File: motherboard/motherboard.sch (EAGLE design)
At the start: 8 parts, among them U1 LED_100V_BUCK, U2 LED_100V_BUCK, U3 LED_100V_BUCK, U4 LED_100V_BUCK

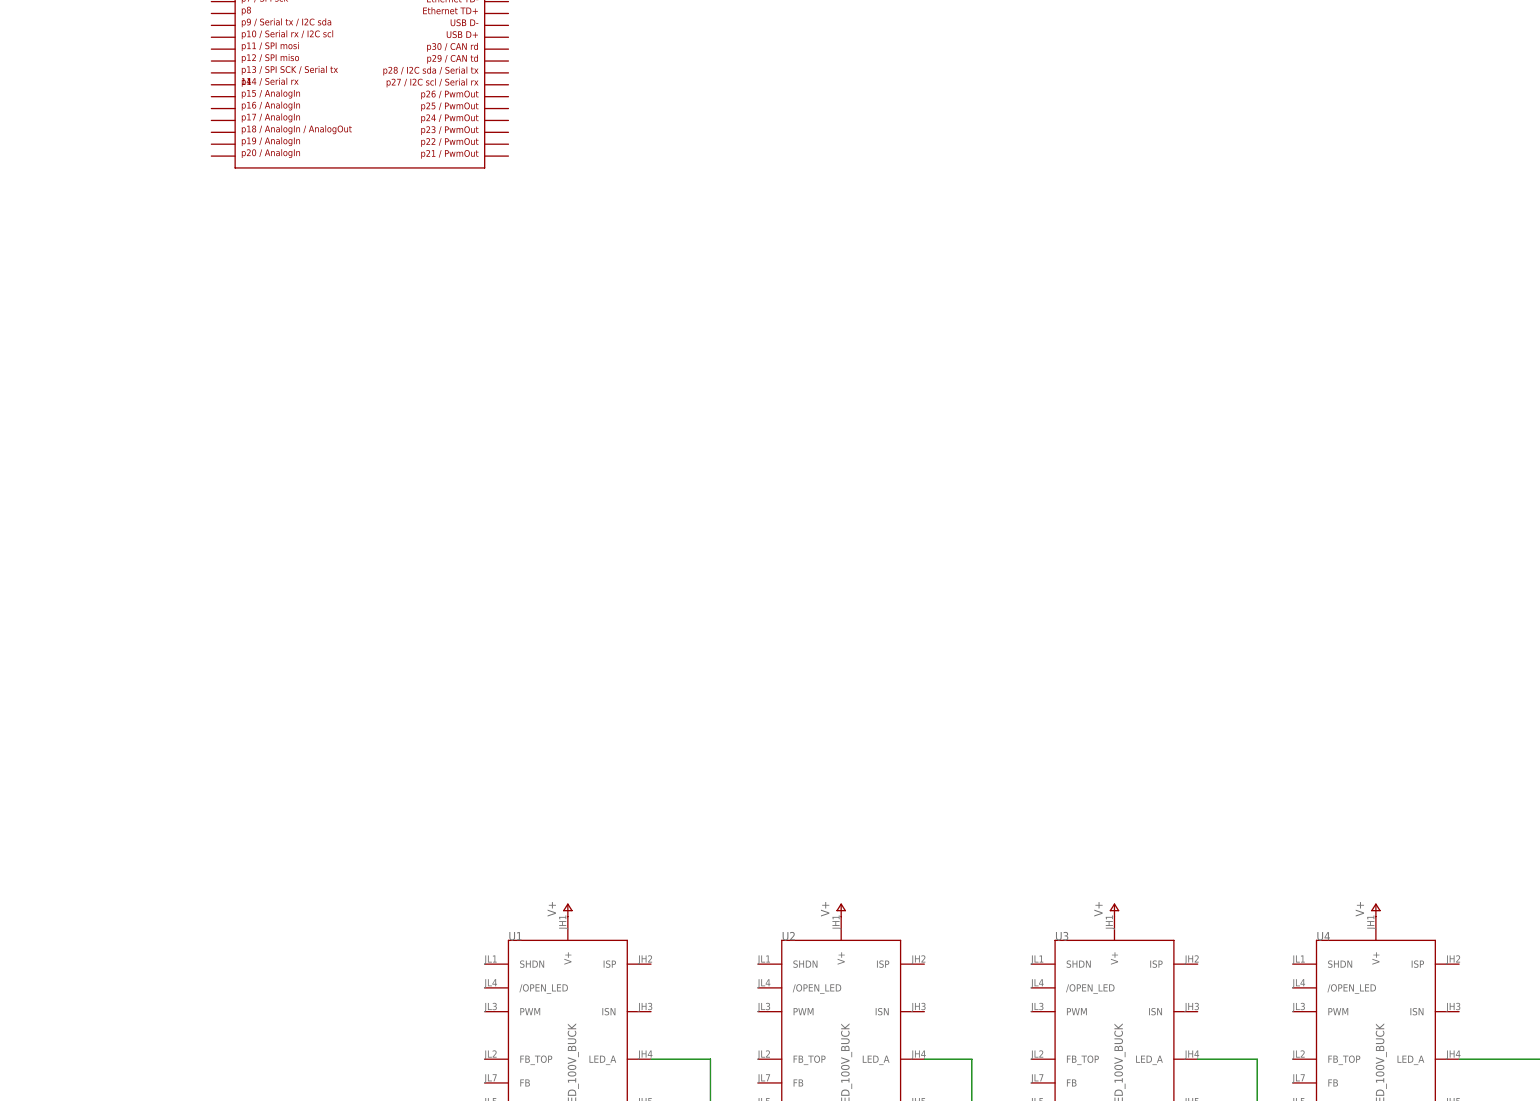
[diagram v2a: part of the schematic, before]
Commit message: Added signals between led drivers and mcu, still need voltage feedback
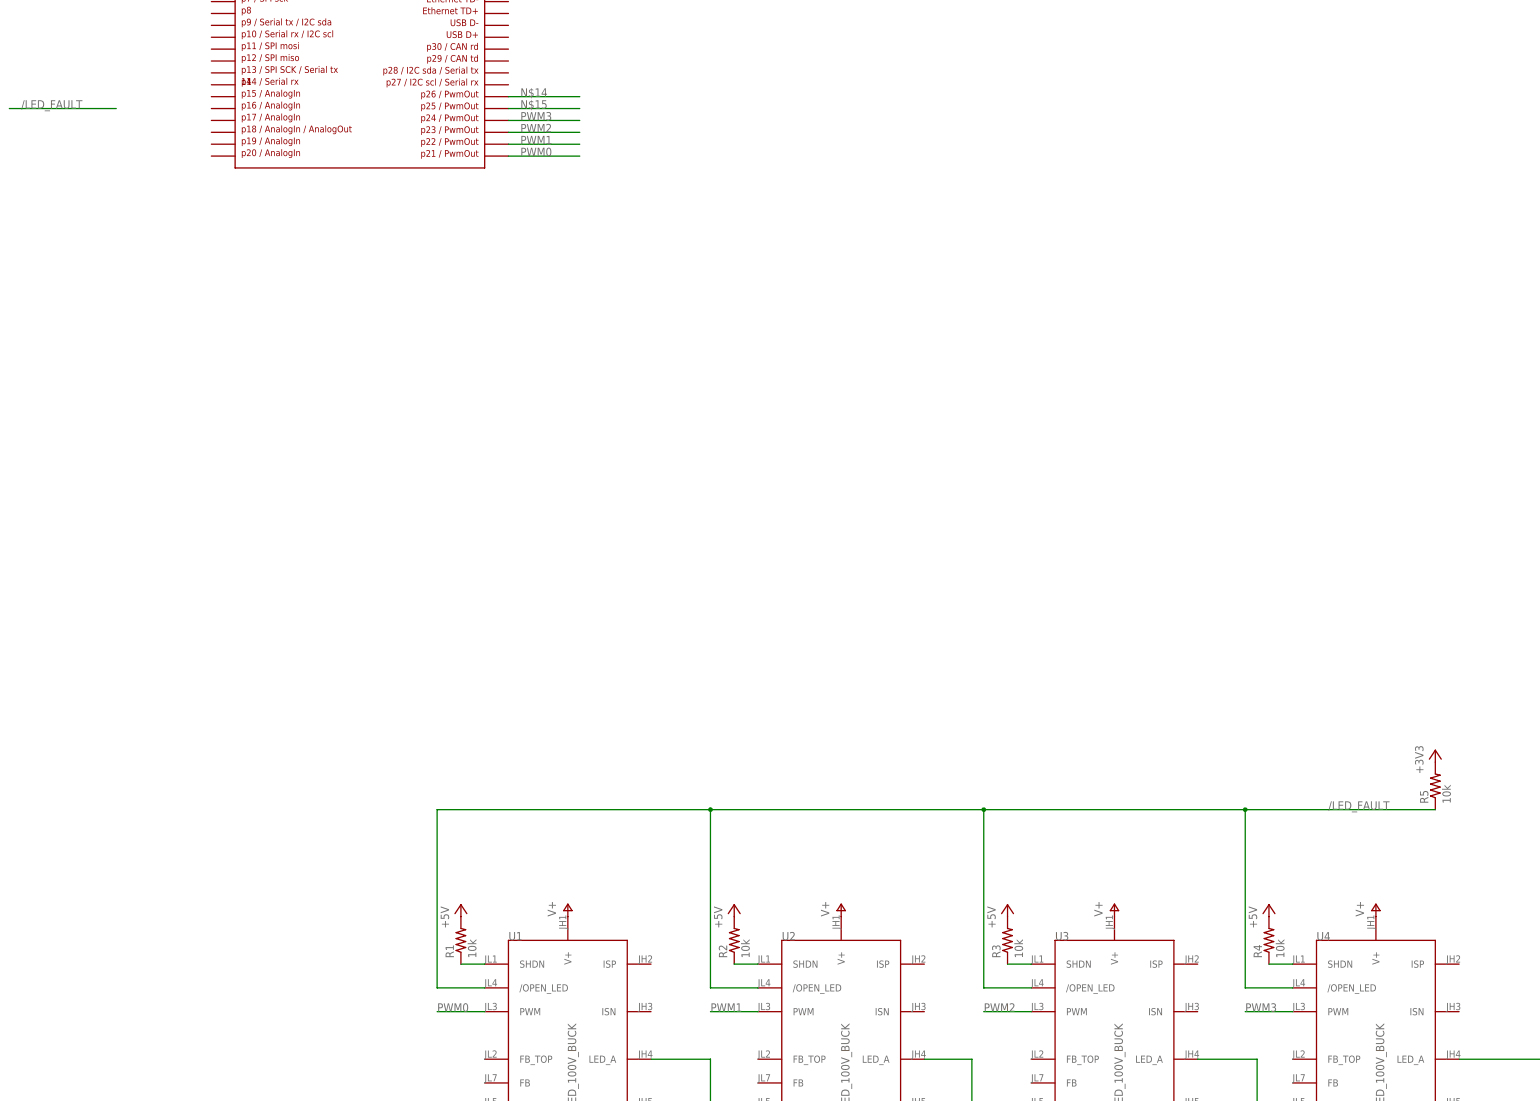
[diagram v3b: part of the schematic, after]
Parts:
- added R1, R2, R3, R4, R5: 10k, rcl:R-US_0204/5
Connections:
- new net /LED_FAULT: R5.1, U1./OPEN_LED, U2./OPEN_LED, U3./OPEN_LED, U4./OPEN_LED
- new net N$10: R1.1, U1.SHDN
- new net N$11: R3.1, U3.SHDN
- new net N$12: R4.1, U4.SHDN
- new net N$13: R2.1, U2.SHDN
- new net N$14: U$1.P$26
- new net N$15: U$1.P$25
- new net PWM0: U$1.P$21, U1.PWM
- new net PWM1: U$1.P$22, U2.PWM
- new net PWM2: U$1.P$23, U3.PWM
- new net PWM3: U$1.P$24, U4.PWM
- net +3V3: now also R5.2
- net +5V: now also R1.2, R2.2, R3.2, R4.2
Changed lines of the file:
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@@
 <?xml version="1.0" encoding="utf-8"?>
 <!DOCTYPE eagle SYSTEM "eagle.dtd">
-<eagle version="6.2">
+<eagle version="6.1">
 <drawing>
 <settings>
@@
 <part name="+3V1" library="supply1" deviceset="+3V3" device=""/>
 <part name="P+6" library="supply1" deviceset="+5V" device=""/>
+<part name="R1" library="rcl" deviceset="R-US_" device="0204/5" value="10k"/>
+<part name="P+1" library="supply1" deviceset="+5V" device=""/>
+<part name="R2" library="rcl" deviceset="R-US_" device="0204/5" value="10k"/>
+<part name="P+7" library="supply1" deviceset="+5V" device=""/>
+<part name="R3" library="rcl" deviceset="R-US_" device="0204/5" value="10k"/>
+<part name="R4" library="rcl" deviceset="R-US_" device="0204/5" value="10k"/>
+<part name="P+8" library="supply1" deviceset="+5V" device=""/>
+<part name="P+9" library="supply1" deviceset="+5V" device=""/>
+<part name="R5" library="rcl" deviceset="R-US_" device="0204/5" value="10k"/>
+<part name="+3V2" library="supply1" deviceset="+3V3" device=""/>
 </parts>
 <sheets>
@@
 <instance part="+3V1" gate="G$1" x="43.18" y="292.1" rot="R270"/>
 <instance part="P+6" gate="1" x="-50.8" y="289.56" rot="R90"/>
+<instance part="R1" gate="G$1" x="15.24" y="76.2" rot="R90"/>
+<instance part="P+1" gate="1" x="15.24" y="83.82"/>
+<instance part="R2" gate="G$1" x="73.66" y="76.2" rot="R90"/>
+<instance part="P+7" gate="1" x="73.66" y="83.82"/>
+<instance part="R3" gate="G$1" x="132.08" y="76.2" rot="R90"/>
+<instance part="R4" gate="G$1" x="187.96" y="76.2" rot="R90"/>
+<instance part="P+8" gate="1" x="132.08" y="83.82"/>
+<instance part="P+9" gate="1" x="187.96" y="83.82"/>
+<instance part="R5" gate="G$1" x="223.52" y="109.22" rot="R90"/>
+<instance part="+3V2" gate="G$1" x="223.52" y="116.84"/>
 </instances>
 <busses>
@@
 <wire x1="40.64" y1="292.1" x2="25.4" y2="292.1" width="0.1524" layer="91"/>
 </segment>
+<segment>
+<pinref part="R5" gate="G$1" pin="2"/>
+<pinref part="+3V2" gate="G$1" pin="+3V3"/>
+</segment>
 </net>
 <net name="+5V" class="0">
@@
 <pinref part="P+6" gate="1" pin="+5V"/>
 </segment>
-</net>
+<segment>
+<pinref part="R1" gate="G$1" pin="2"/>
+<pinref part="P+1" gate="1" pin="+5V"/>
+</segment>
+<segment>
+<pinref part="R2" gate="G$1" pin="2"/>
+<pinref part="P+7" gate="1" pin="+5V"/>
+</segment>
+<segment>
+<pinref part="R3" gate="G$1" pin="2"/>
+<pinref part="P+8" gate="1" pin="+5V"/>
+</segment>
+<segment>
+<pinref part="R4" gate="G$1" pin="2"/>
+<pinref part="P+9" gate="1" pin="+5V"/>
+</segment>
+</net>
+<net name="N$10" class="0">
+<segment>
+<pinref part="U1" gate="G$1" pin="SHDN"/>
+<pinref part="R1" gate="G$1" pin="1"/>
+<wire x1="15.24" y1="71.12" x2="20.32" y2="71.12" width="0.1524" layer="91"/>
+</segment>
+</net>
+<net name="N$11" class="0">
+<segment>
+<pinref part="U3" gate="G$1" pin="SHDN"/>
+<pinref part="R3" gate="G$1" pin="1"/>
+<wire x1="132.08" y1="71.12" x2="137.16" y2="71.12" width="0.1524" layer="91"/>
+</segment>
+</net>
+<net name="N$12" class="0">
+<segment>
+<pinref part="U4" gate="G$1" pin="SHDN"/>
+<pinref part="R4" gate="G$1" pin="1"/>
+<wire x1="187.96" y1="71.12" x2="193.04" y2="71.12" width="0.1524" layer="91"/>
+</segment>
+</net>
+<net name="N$13" class="0">
+<segment>
+<pinref part="R2" gate="G$1" pin="1"/>
+<pinref part="U2" gate="G$1" pin="SHDN"/>
+<wire x1="73.66" y1="71.12" x2="78.74" y2="71.12" width="0.1524" layer="91"/>
+</segment>
+</net>
+<net name="/LED_FAULT" class="0">
+<segment>
+<pinref part="U3" gate="G$1" pin="/OPEN_LED"/>
+<wire x1="137.16" y1="66.04" x2="127" y2="66.04" width="0.1524" layer="91"/>
+<wire x1="127" y1="66.04" x2="127" y2="104.14" width="0.1524" layer="91"/>
+<pinref part="R5" gate="G$1" pin="1"/>
+<wire x1="223.52" y1="104.14" x2="182.88" y2="104.14" width="0.1524" layer="91"/>
+<pinref part="U4" gate="G$1" pin="/OPEN_LED"/>
+<wire x1="182.88" y1="104.14" x2="127" y2="104.14" width="0.1524" layer="91"/>
+<wire x1="193.04" y1="66.04" x2="182.88" y2="66.04" width="0.1524" layer="91"/>
+<wire x1="182.88" y1="66.04" x2="182.88" y2="104.14" width="0.1524" layer="91"/>
+<pinref part="U2" gate="G$1" pin="/OPEN_LED"/>
+<wire x1="78.74" y1="66.04" x2="68.58" y2="66.04" width="0.1524" layer="91"/>
+<wire x1="68.58" y1="66.04" x2="68.58" y2="104.14" width="0.1524" layer="91"/>
+<wire x1="68.58" y1="104.14" x2="127" y2="104.14" width="0.1524" layer="91"/>
+<pinref part="U1" gate="G$1" pin="/OPEN_LED"/>
+<wire x1="20.32" y1="66.04" x2="10.16" y2="66.04" width="0.1524" layer="91"/>
+<wire x1="10.16" y1="66.04" x2="10.16" y2="104.14" width="0.1524" layer="91"/>
+<wire x1="10.16" y1="104.14" x2="68.58" y2="104.14" width="0.1524" layer="91"/>
+<junction x="68.58" y="104.14"/>
+<junction x="127" y="104.14"/>
+<junction x="182.88" y="104.14"/>
+<label x="200.66" y="104.14" size="1.778" layer="95"/>
+</segment>
+<segment>
+<wire x1="-81.28" y1="254" x2="-58.42" y2="254" width="0.1524" layer="91"/>
+<label x="-78.74" y="254" size="1.778" layer="95"/>
+</segment>
+</net>
+<net name="PWM0" class="0">
+<segment>
+<pinref part="U1" gate="G$1" pin="PWM"/>
+<wire x1="20.32" y1="60.96" x2="10.16" y2="60.96" width="0.1524" layer="91"/>
+<label x="10.16" y="60.96" size="1.778" layer="95"/>
+</segment>
+<segment>
+<pinref part="U$1" gate="G$1" pin="P$21"/>
+<wire x1="25.4" y1="243.84" x2="40.64" y2="243.84" width="0.1524" layer="91"/>
+<label x="27.94" y="243.84" size="1.778" layer="95"/>
+</segment>
+</net>
+<net name="PWM1" class="0">
+<segment>
+<pinref part="U2" gate="G$1" pin="PWM"/>
+<wire x1="78.74" y1="60.96" x2="68.58" y2="60.96" width="0.1524" layer="91"/>
+<label x="68.58" y="60.96" size="1.778" layer="95"/>
+</segment>
+<segment>
+<pinref part="U$1" gate="G$1" pin="P$22"/>
+<wire x1="25.4" y1="246.38" x2="40.64" y2="246.38" width="0.1524" layer="91"/>
+<label x="27.94" y="246.38" size="1.778" layer="95"/>
+</segment>
+</net>
+<net name="PWM2" class="0">
+<segment>
+<pinref part="U3" gate="G$1" pin="PWM"/>
+<wire x1="137.16" y1="60.96" x2="127" y2="60.96" width="0.1524" layer="91"/>
+<label x="127" y="60.96" size="1.778" layer="95"/>
+</segment>
+<segment>
+<pinref part="U$1" gate="G$1" pin="P$23"/>
+<wire x1="25.4" y1="248.92" x2="40.64" y2="248.92" width="0.1524" layer="91"/>
+<label x="27.94" y="248.92" size="1.778" layer="95"/>
+</segment>
+</net>
+<net name="PWM3" class="0">
+<segment>
+<pinref part="U4" gate="G$1" pin="PWM"/>
+<wire x1="193.04" y1="60.96" x2="182.88" y2="60.96" width="0.1524" layer="91"/>
+<label x="182.88" y="60.96" size="1.778" layer="95"/>
+</segment>
+<segment>
+<pinref part="U$1" gate="G$1" pin="P$24"/>
+<wire x1="25.4" y1="251.46" x2="40.64" y2="251.46" width="0.1524" layer="91"/>
+<label x="27.94" y="251.46" size="1.778" layer="95"/>
+</segment>
+</net>
+<net name="N$14" class="0">
+<segment>
+<pinref part="U$1" gate="G$1" pin="P$26"/>
+<wire x1="25.4" y1="256.54" x2="40.64" y2="256.54" width="0.1524" layer="91"/>
+<label x="27.94" y="256.54" size="1.778" layer="95"/>
+</segment>
+</net>
+<net name="N$15" class="0">
+<segment>
+<pinref part="U$1" gate="G$1" pin="P$25"/>
+<wire x1="25.4" y1="254" x2="40.64" y2="254" width="0.1524" layer="91"/>
+<label x="27.94" y="254" size="1.778" layer="95"/>
+</segment>
+</net>

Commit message: Complete schematic
This commit uses generic part selections and has no board layout yet.
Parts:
- added BREAKS, CA: (no value), con-amp-quick:M06
- added C1, C2: (no value), rcl:C-US050-024X044
- added CADENCE, DC, FET, REGEN, SPEED: (no value), con-amp-quick:M02
- added D1, D2: 3.3V, SparkFun-DiscreteSemi:DIODE-ZENERPTH
- added F1, F2: (no value), special:FUSE
- added GRIP: (no value), con-amp-quick:M05
- added IC1: USB6B1, st-microelectronics:USB6B1
- added IR, PHOTO, UART: (no value), con-amp-quick:M04
- added MISSILE: (no value), SparkFun-Electromechanical:SWITCH-SPDTPTH
- added OA1: LM358, SparkFun-AnalogIC:LM358
- added Q1: MOSFET-NCHANNELPTH2, SparkFun-DiscreteSemi:MOSFET-NCHANNELPTH2
- added R10: 50K, rcl:R-US_0204/5
- added R11, R12, R6, R7: 5k, rcl:R-US_0204/5
- added R13, R14: 1k, rcl:R-US_0204/5
- added R15, R16, R17: 10k, rcl:R-US_0204/5
- added R8, R9: 100k, SparkFun-Electromechanical:TRIMPOT3362U-2
- added S2, S3: (no value), SparkFun-Electromechanical:TAC_SWITCHPTH
- added SONAR: M05X2PTH, SparkFun-Connectors:M05X2PTH
- added T1, T2: 2N3904, transistor:2N3904
- added X1: USB_3P-85-32003-00X-1, con-cypressindustries:USB_3P-85-32003-00X-1
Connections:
- removed net N$15: U$1.P$25
- new net BATT_SENSE: D1.C, R11.2, R12.1, U$1.P$16
- new net BREAK_L: BREAKS.2, U$1.P$19
- new net BREAK_R: BREAKS.5, U$1.P$20
- new net BTN1: S2.1, S2.2, U$1.P$30
- new net BTN2: S3.1, S3.2, U$1.P$29
- new net CADENCE: CADENCE.1
- new net D+: IC1.IO2@2, U$1.P$31, X1C.3
- new net D-: IC1.IO1@2, U$1.P$32, X1C.2
- new net GRIP_PB: GRIP.4
- new net GRIP_THROTTLE: GRIP.2, U$1.P$17
- new net MOT_CUR: D2.C, OA1G$1.OUT, R8.CW, U$1.P$15
- new net N$16: OA1G$1.-IN, R6.1, R8.WIPER
- new net N$17: OA1G$1.+IN, R7.1
- new net N$18: R10.1, R9.WIPER
- new net N$19: MISSILE.O, OA1G$2.OUT, R9.CW
- new net N$20: OA1G$2.-IN
- new net N$21: F1.2, R11.1
- new net N$22: C2.1, PHOTO.3, R13.2
- new net N$23: C1.1, PHOTO.1, R14.2
- new net N$24: DC.2, F2.1
- new net N$25: REGEN.1, T1.C
- new net N$26: FET.1, Q1.D
- new net PHOTO1: R14.1
- new net PHOTO2: R13.1
- new net REGEN: T1.B, U$1.P$26
- new net SCL: IR.1, R16.2, U$1.P$27
- new net SDA: IR.2, R15.2, U$1.P$28
- new net SERIAL_RX: U$1.P$14, UART.2
- new net SERIAL_TX: U$1.P$13, UART.3
- new net SERVO_PWM: T2.B, U$1.P$25
- new net SHUNT+: CA.4, R7.2
- new net SHUNT-: CA.3, R6.2
- new net SONAR_PULSE1: SONAR.3, U$1.P$11
- new net SONAR_PULSE2: SONAR.4, U$1.P$12
- new net SONAR_TRIGGER1: SONAR.5, SONAR.8
- new net SONAR_TRIGGER2: SONAR.6, SONAR.7
- new net SPEED: SPEED.1
- new net TACHOMETER: CA.5
- new net THROTTLE_OUT: CA.6, MISSILE.P
- new net THROTTLE_OUT_RAW: OA1G$2.+IN, U$1.P$18
- new net VBATT: CA.1, F1.1
- new net VU: IC1.VCC@2, U$1.P$39, X1C.1
- net +3V3: now also BREAKS.1, BREAKS.4, GRIP.1, IR.3, R15.1, R16.1, S2.3, S2.4, S3.3, S3.4, UART.1
- net +5V: now also F2.2, OA1G$1.V+, SONAR.1, SONAR.2, T2.C, X1A.1, X1B.1
- net GND: now also BREAKS.3, BREAKS.6, C1.2, C2.2, CA.2, CADENCE.2, D1.A, D2.A, DC.1, FET.2, GRIP.3, GRIP.5, IC1.GND@2, IR.4, MISSILE.S, OA1G$1.V-, PHOTO.2, PHOTO.4, Q1.S, R10.2, R12.2, R17.1, REGEN.2, SONAR.10, SONAR.9, SPEED.2, T1.E, UART.4, X1A.4, X1B.4, X1C.4
- net N$14: now also Q1.G, R17.2, T2.E; no longer U$1.P$26
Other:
- moved on the sheet: R1, R2, R3, R4, R5, U$3, U1, U2, U3, U4

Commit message: Ready for parts and firmware
Far enough along now to determine the size of the perfboard to put this
on (6" x 6") and to start working on a BOM and firmware. My plan now is
to get a little ways in to the firmware and place the order when I'm
sure the firmware won't require hardware design changes.
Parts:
- removed BREAKS: (no value), con-amp-quick:M06
- removed S1: (no value), SparkFun-Electromechanical:TAC_SWITCHPTH
- added PTC1, PTC2, PTC3: (no value), ptc-ntc:PTC679
- added X_BREAK_L, X_BREAK_R: (no value), SparkFun-Connectors:M03JST-PTH
- CADENCE, DC, FET, REGEN, SPEED: device con-amp-quick:M02 -> SparkFun-Connectors:M02JST-PTH-2-KIT
- F1: value (none) -> PTCPTH; device special:FUSE -> SparkFun-PowerIC:PTCPTH
- PHOTO, UART: device con-amp-quick:M04 -> SparkFun-Connectors:M04JST-PTH
- renumbered U$3 to LEDS
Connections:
- new net N$15: PTC2.2, X1A.1
- new net N$27: PTC3.2, X1B.1
- net +3V3: now also UART.4, X_BREAK_L.3, X_BREAK_R.3; no longer BREAKS.1, BREAKS.4, UART.1
- net +5V: now also PTC2.1, PTC3.1; no longer X1A.1, X1B.1
- net BREAK_L: now also X_BREAK_L.2; no longer BREAKS.2
- net BREAK_R: now also X_BREAK_R.2; no longer BREAKS.5
- net CADENCE: now also CADENCE.2; no longer CADENCE.1
- net GND: now also CADENCE.1, PHOTO.1, PHOTO.3, SPEED.1, UART.1, X_BREAK_L.1, X_BREAK_R.1; no longer BREAKS.3, BREAKS.6, CADENCE.2, PHOTO.2, PHOTO.4, S1.1, S1.2, SPEED.2, UART.4
- net N$1: now also PTC1.2, X1C.1; no longer S1.3, S1.4, U$1.P$3
- net N$22: now also PHOTO.2; no longer PHOTO.3
- net N$23: now also PHOTO.4; no longer PHOTO.1
- net SERIAL_RX: now also UART.3; no longer UART.2
- net SERIAL_TX: now also UART.2; no longer UART.3
- net SPEED: now also SPEED.2; no longer SPEED.1
- net VU: now also PTC1.1; no longer X1C.1
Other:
- moved on the sheet: CADENCE, PHOTO, SPEED, UART
